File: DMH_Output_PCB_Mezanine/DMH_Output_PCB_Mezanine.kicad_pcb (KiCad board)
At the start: 2 copper layers, 49 x 175 mm, 105 parts, among them J30 Conn_01x04_PinHeader, J32 Conn_01x06_PinHeader, J33 Conn_01x06, J34 Conn_01x06, J37 Conn_01x06, J38 Conn_01x06, J39 Conn_01x02_PinHeader, J40 Conn_01x02_PinHeader, U10 NE5532, U16 NE5532, U17 NE5532, U18 NE5532, U19 NE5532, U7 TL072, U9 NE5532

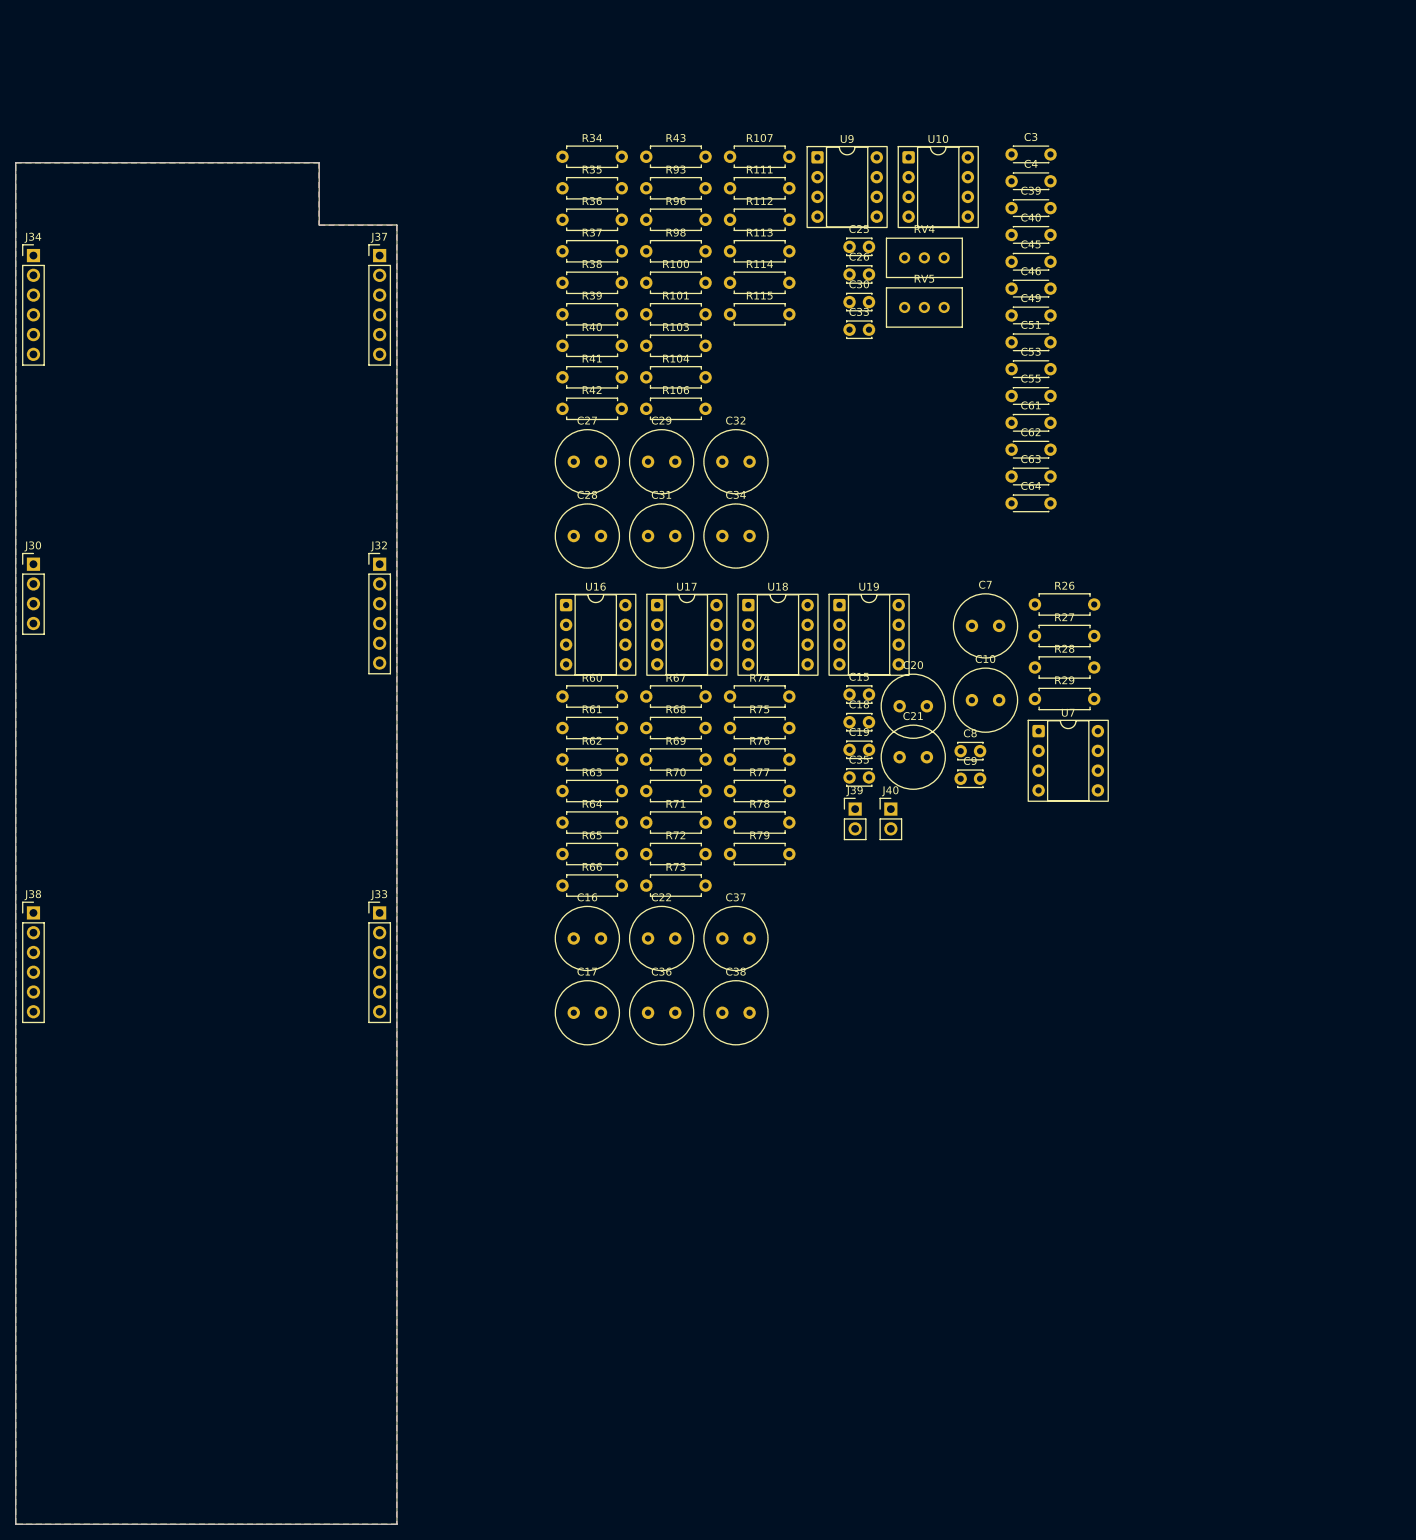
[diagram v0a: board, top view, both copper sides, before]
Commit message: Defined Mezanine PCB outer limits
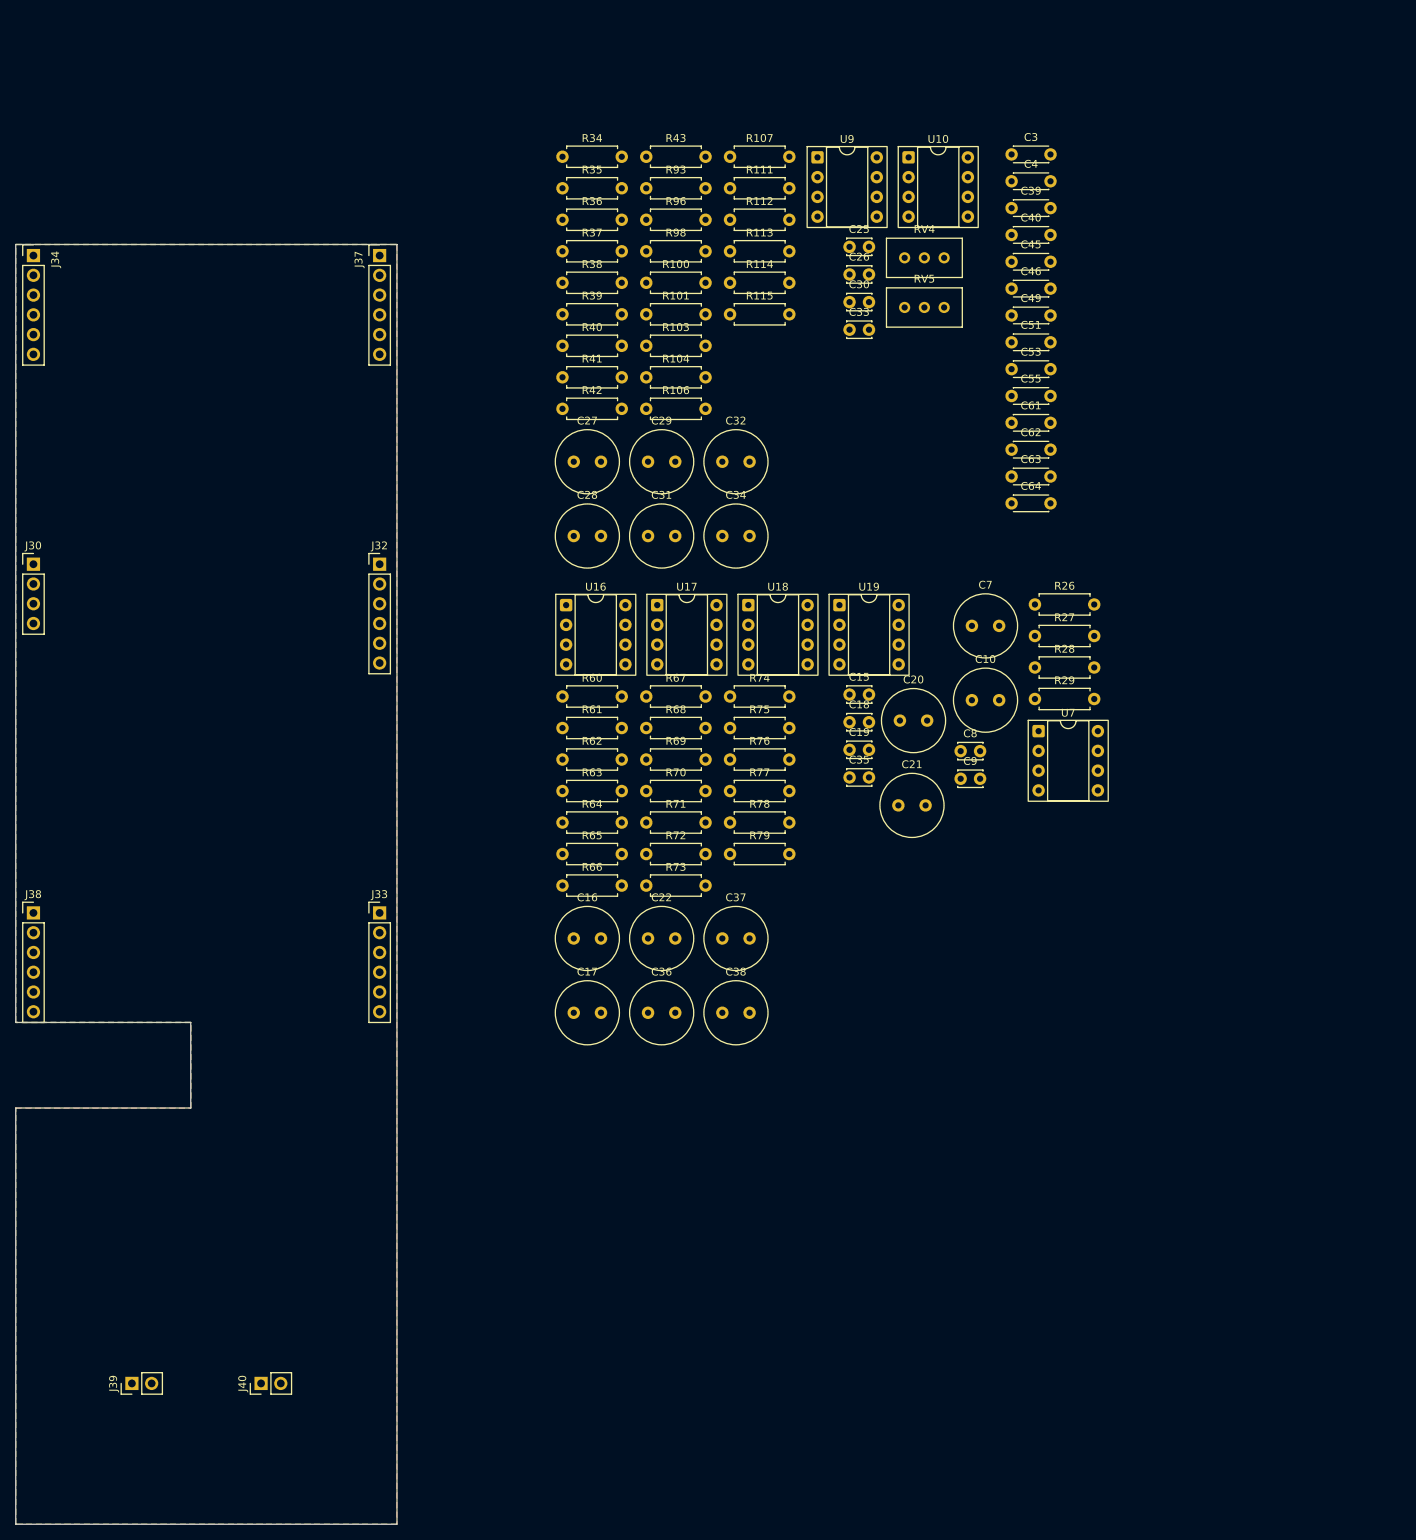
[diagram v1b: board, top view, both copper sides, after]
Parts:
- moved J39 118.7 mm to (65.4, 199.4), turned to 90 degrees
- moved J40 109.6 mm to (82.0, 199.4), turned to 90 degrees
- moved C21 6.20 mm to (163.9, 125.1)
- moved C20 1.85 mm to (164.2, 114.2)
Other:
- board size 49 x 175 mm -> 49 x 164.5 mm
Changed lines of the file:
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@@
 	)
 	(footprint "Connector_PinHeader_2.54mm:PinHeader_1x02_P2.54mm_Vertical"
+		(locked yes)
 		(layer "F.Cu")
-		(at 162.985 125.575)
+		(at 82.03 199.4 90)
 		(descr "Through hole straight pin header, 1x02, 2.54mm pitch, single row")
 		(tags "Through hole pin header THT 1x02 2.54mm single row")
 		(property "Reference" "J40"
-			(at 0 -2.38 0)
+			(at 0 -2.38 90)
 			(layer "F.SilkS")
 			(effects
@@
 		)
 		(property "Value" "Conn_01x02_PinHeader"
-			(at 0 4.92 0)
+			(at 0 4.92 90)
 			(layer "F.Fab")
 			(hide yes)
@@
 		)
 		(property "Datasheet" ""
-			(at 0 0 0)
+			(at 0 0 90)
 			(layer "F.Fab")
 			(hide yes)
@@
 		)
 		(property "Description" "Generic connector, single row, 01x02"
-			(at 0 0 0)
+			(at 0 0 90)
 			(layer "F.Fab")
 			(hide yes)
@@
 		)
 		(property "KiLib_Generator" "connector/pin_header_socket"
-			(at 0 0 0)
+			(at 0 0 90)
 			(layer "F.SilkS")
 			(hide yes)
@@
 		)
 		(fp_line
-			(start -1.38 1.27)
-			(end -1.38 3.92)
+			(start 1.38 1.27)
+			(end 1.38 3.92)
 			(stroke
 				(width 0.12)
@@
 		)
 		(fp_line
-			(start -1.38 3.92)
-			(end 1.38 3.92)
+			(start -1.38 1.27)
+			(end -1.38 3.92)
 			(stroke
 				(width 0.12)
@@
 		)
 		(fp_line
-			(start 1.38 1.27)
+			(start -1.38 3.92)
 			(end 1.38 3.92)
 			(stroke
@@
 		)
 		(fp_line
-			(start -1.27 -0.635)
-			(end -0.635 -1.27)
+			(start 1.27 -1.27)
+			(end 1.27 3.81)
 			(stroke
 				(width 0.1)
@@
 		)
 		(fp_line
-			(start -1.27 3.81)
-			(end -1.27 -0.635)
+			(start -0.635 -1.27)
+			(end 1.27 -1.27)
 			(stroke
 				(width 0.1)
@@
 		)
 		(fp_line
-			(start -0.635 -1.27)
-			(end 1.27 -1.27)
+			(start -1.27 -0.635)
+			(end -0.635 -1.27)
 			(stroke
 				(width 0.1)
@@
 		)
 		(fp_line
-			(start 1.27 -1.27)
-			(end 1.27 3.81)
+			(start 1.27 3.81)
+			(end -1.27 3.81)
 			(stroke
 				(width 0.1)
@@
 		)
 		(fp_line
-			(start 1.27 3.81)
-			(end -1.27 3.81)
+			(start -1.27 3.81)
+			(end -1.27 -0.635)
 			(stroke
 				(width 0.1)
@@
 		)
 		(fp_text user "${REFERENCE}"
-			(at 0 1.27 90)
+			(at 0 1.27 0)
 			(layer "F.Fab")
 			(effects
@@
 		)
 		(pad "1" thru_hole rect
-			(at 0 0)
+			(at 0 0 90)
 			(size 1.7 1.7)
 			(drill 1)
@@
 		)
 		(pad "2" thru_hole circle
-			(at 0 2.54)
+			(at 0 2.54 90)
 			(size 1.7 1.7)
 			(drill 1)
@@
 	(footprint "Capacitor_THT:C_Radial_D8.0mm_H11.5mm_P3.50mm"
 		(layer "F.Cu")
-		(at 164.114775 118.905)
+		(at 163.95 125.1)
 		(descr "C, Radial series, Radial, pin pitch=3.50mm, diameter=8mm, height=11.5mm, Non-Polar Electrolytic Capacitor")
 		(tags "C Radial series Radial pin pitch 3.50mm diameter 8mm height 11.5mm Non-Polar Electrolytic Capacitor")
@@
 		(tags "Through hole pin header THT 1x06 2.54mm single row")
 		(property "Reference" "J37"
-			(at 0 -2.38 0)
+			(at -2.675 0.475 90)
 			(layer "F.SilkS")
 			(effects
@@
 		(tags "Through hole pin header THT 1x06 2.54mm single row")
 		(property "Reference" "J34"
-			(at 0 -2.38 0)
+			(at 2.825 0.475 90)
 			(layer "F.SilkS")
 			(effects
@@
 	)
 	(footprint "Connector_PinHeader_2.54mm:PinHeader_1x02_P2.54mm_Vertical"
+		(locked yes)
 		(layer "F.Cu")
-		(at 158.395 125.575)
+		(at 65.43 199.4 90)
 		(descr "Through hole straight pin header, 1x02, 2.54mm pitch, single row")
 		(tags "Through hole pin header THT 1x02 2.54mm single row")
 		(property "Reference" "J39"
-			(at 0 -2.38 0)
+			(at 0 -2.38 90)
 			(layer "F.SilkS")
 			(effects
@@
 		)
 		(property "Value" "Conn_01x02_PinHeader"
-			(at 0 4.92 0)
+			(at 0 4.92 90)
 			(layer "F.Fab")
 			(hide yes)
@@
 		)
 		(property "Datasheet" ""
-			(at 0 0 0)
+			(at 0 0 90)
 			(layer "F.Fab")
 			(hide yes)
@@
 		)
 		(property "Description" "Generic connector, single row, 01x02"
-			(at 0 0 0)
+			(at 0 0 90)
 			(layer "F.Fab")
 			(hide yes)
@@
 		)
 		(property "KiLib_Generator" "connector/pin_header_socket"
-			(at 0 0 0)
+			(at 0 0 90)
 			(layer "F.SilkS")
 			(hide yes)
@@
 		)
 		(fp_line
-			(start -1.38 1.27)
-			(end -1.38 3.92)
+			(start 1.38 1.27)
+			(end 1.38 3.92)
 			(stroke
 				(width 0.12)
@@
 		)
 		(fp_line
-			(start -1.38 3.92)
-			(end 1.38 3.92)
+			(start -1.38 1.27)
+			(end -1.38 3.92)
 			(stroke
 				(width 0.12)
@@
 		)
 		(fp_line
-			(start 1.38 1.27)
+			(start -1.38 3.92)
 			(end 1.38 3.92)
 			(stroke
@@
 		)
 		(fp_line
-			(start -1.27 -0.635)
-			(end -0.635 -1.27)
+			(start 1.27 -1.27)
+			(end 1.27 3.81)
 			(stroke
 				(width 0.1)
@@
 		)
 		(fp_line
-			(start -1.27 3.81)
-			(end -1.27 -0.635)
+			(start -0.635 -1.27)
+			(end 1.27 -1.27)
 			(stroke
 				(width 0.1)
@@
 		)
 		(fp_line
-			(start -0.635 -1.27)
-			(end 1.27 -1.27)
+			(start -1.27 -0.635)
+			(end -0.635 -1.27)
 			(stroke
 				(width 0.1)
@@
 		)
 		(fp_line
-			(start 1.27 -1.27)
-			(end 1.27 3.81)
+			(start 1.27 3.81)
+			(end -1.27 3.81)
 			(stroke
 				(width 0.1)
@@
 		)
 		(fp_line
-			(start 1.27 3.81)
-			(end -1.27 3.81)
+			(start -1.27 3.81)
+			(end -1.27 -0.635)
 			(stroke
 				(width 0.1)
@@
 		)
 		(fp_text user "${REFERENCE}"
-			(at 0 1.27 90)
+			(at 0 1.27 0)
 			(layer "F.Fab")
 			(effects
@@
 		)
 		(pad "1" thru_hole rect
-			(at 0 0)
+			(at 0 0 90)
 			(size 1.7 1.7)
 			(drill 1)
@@
 		)
 		(pad "2" thru_hole circle
-			(at 0 2.54)
+			(at 0 2.54 90)
 			(size 1.7 1.7)
 			(drill 1)
@@
 	(footprint "Capacitor_THT:C_Radial_D8.0mm_H11.5mm_P3.50mm"
 		(layer "F.Cu")
-		(at 164.114775 112.355)
+		(at 164.15 114.2)
 		(descr "C, Radial series, Radial, pin pitch=3.50mm, diameter=8mm, height=11.5mm, Non-Polar Electrolytic Capacitor")
 		(tags "C Radial series Radial pin pitch 3.50mm diameter 8mm height 11.5mm Non-Polar Electrolytic Capacitor")
@@
 	)
 	(gr_line
-		(start 50.5 42.5)
-		(end 89.5 42.5)
+		(start 50.5 53)
+		(end 99.5 53)
+		(stroke
+			(width 0.05)
+			(type default)
+		)
+		(layer "Edge.Cuts")
+	)
+	(gr_line
+		(start 50.5 153)
+		(end 50.5 53)
+		(stroke
+			(width 0.05)
+			(type default)
+		)
+		(layer "Edge.Cuts")
+	)
+	(gr_line
+		(start 50.5 153)
+		(end 73 153)
 		(stroke
 			(width 0.05)
@@
 	(gr_line
 		(start 50.5 217.5)
-		(end 50.5 42.5)
+		(end 50.5 164)
 		(stroke
 			(width 0.05)
@@
 	)
 	(gr_line
-		(start 89.5 42.5)
-		(end 89.5 50.5)
+		(start 73 153)
+		(end 73 164)
 		(stroke
 			(width 0.05)
@@
 	)
 	(gr_line
-		(start 89.5 50.5)
-		(end 99.5 50.5)
+		(start 73 164)
+		(end 50.5 164)
 		(stroke
 			(width 0.05)
@@
 	)
 	(gr_line
-		(start 99.5 50.5)
+		(start 99.5 53)
 		(end 99.5 217.5)
 		(stroke
@@
 		(net "GND")
 		(layers "F.Cu" "B.Cu")
-		(name "Ground_planes")
+		(name "Ground_planes")
 		(hatch edge 0.5)
 		(connect_pads
@@
 		(polygon
 			(pts
-				(xy 50.5 42.5) (xy 89.5 42.5) (xy 89.5 50.5) (xy 99.5 50.5) (xy 99.5 217.5) (xy 50.5 217.5)
+				(xy 50.5 53) (xy 99.5 53) (xy 99.5 217.5) (xy 50.5 217.5) (xy 50.5 164) (xy 73 164) (xy 73 153)
+				(xy 50.5 153)
 			)
 		)

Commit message: Placed PreAmp components on PCB
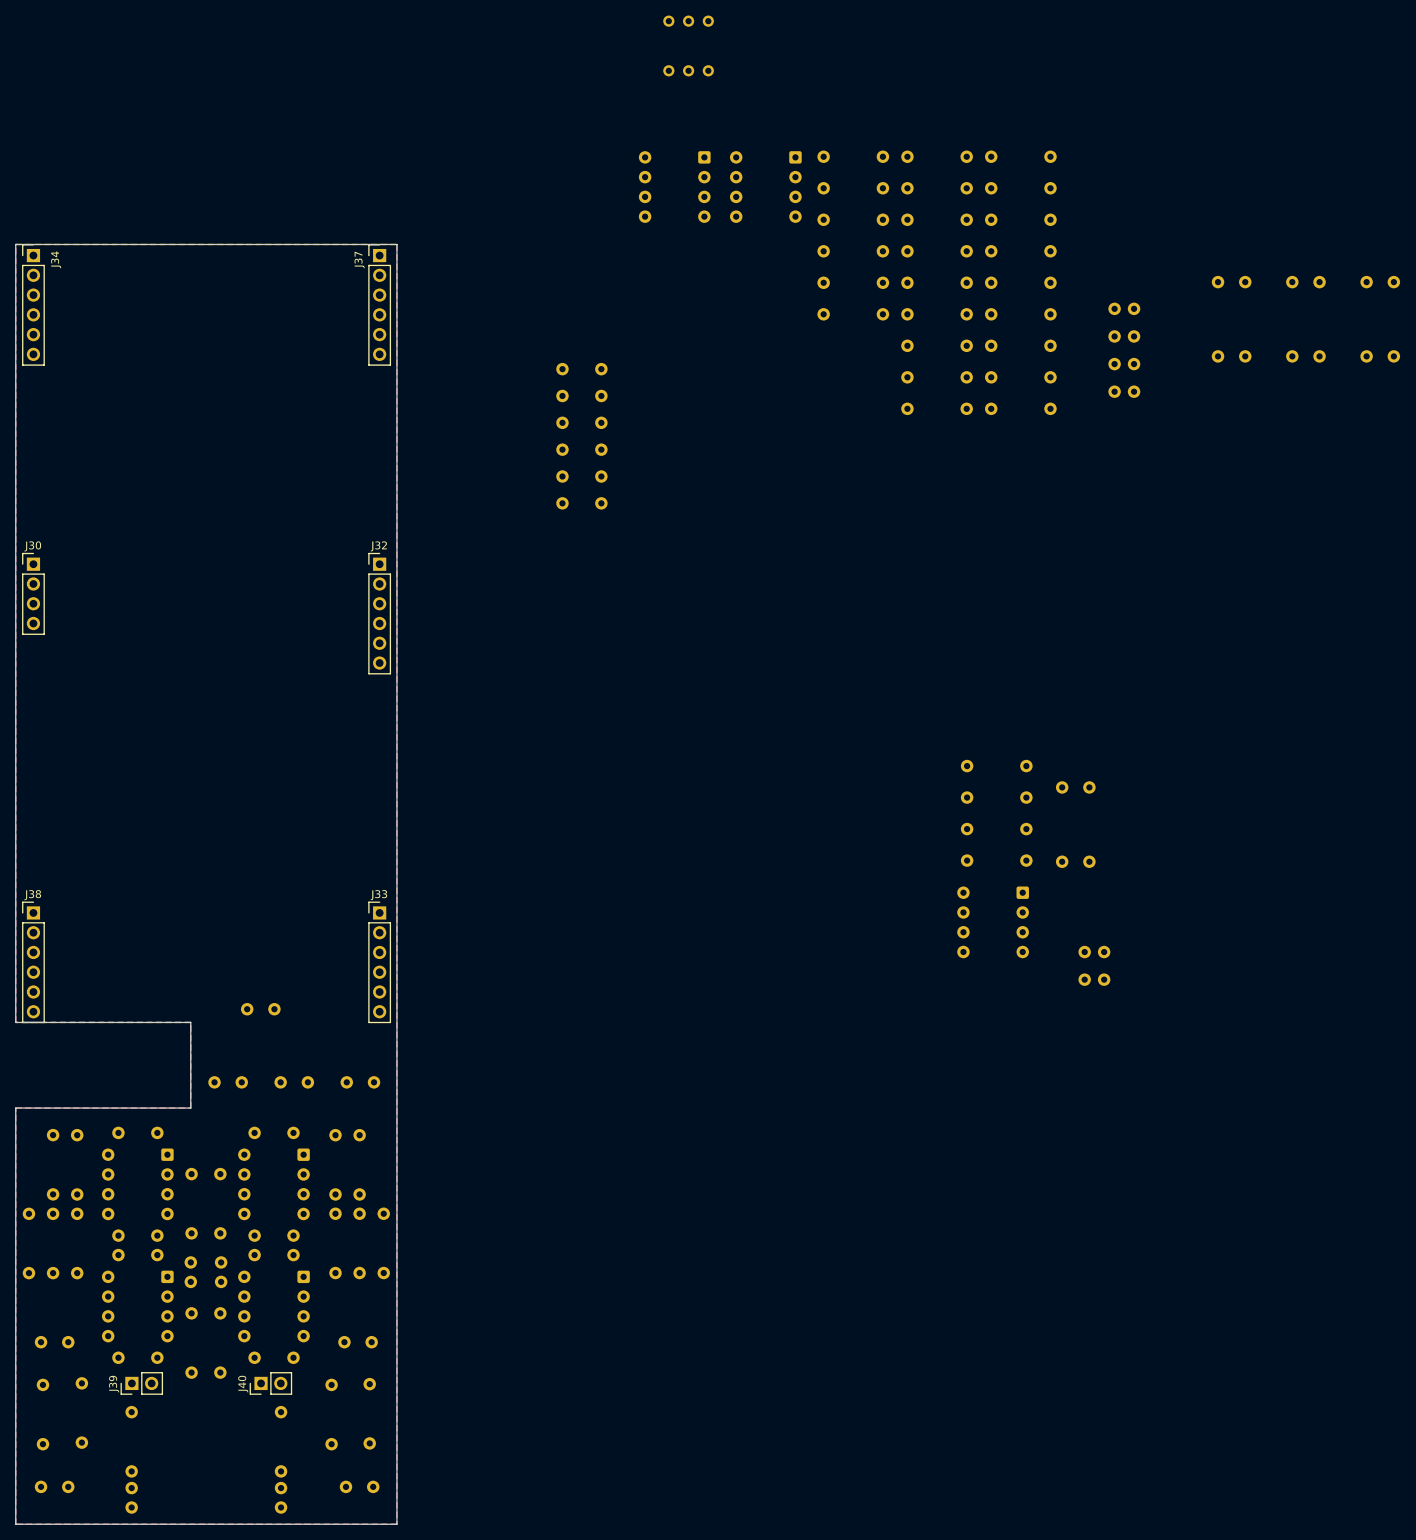
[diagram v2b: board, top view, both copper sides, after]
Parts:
- C10, C15, C16, C17, C18, C19, C20, C21, C22, C25, C26, C27, C28, C29, C3, C30, C31, C32, C33, C34, C35, C36, C37, C38, C39, C4, C40, C45, C46, C49, C51, C53, C55, C61, C62, C63, C64, C7, C8, C9, R100, R101, R103, R104, R106, R107, R111, R112, R113, R114, R115, R26, R27, R28, R29, R34, R35, R36, R37, R38, R39, R40, R41, R42, R43, R60, R61, R62, R63, R64, R65, R66, R67, R68, R69, R70, R71, R72, R73, R74, R75, R76, R77, R78, R79, R93, R96, R98, RV4, RV5, U10, U16, U17, U18, U19, U7, U9: moved to B.Cu
- moved C40 184.4 mm to (63.7, 196.1)
- moved C4 177.6 mm to (63.7, 180.4)
- moved C39 176.9 mm to (63.7, 182.9)
- moved C3 170.3 mm to (63.7, 167.2)
- moved C51 162.8 mm to (81.2, 196.1)
- moved C46 155.8 mm to (81.2, 180.4)
- moved C49 155.1 mm to (81.2, 182.9)
- moved C45 148.3 mm to (81.2, 167.2)
- moved C18 136.8 mm to (65.4, 215.3), turned to 90 degrees
- moved C15 127.5 mm to (84.6, 215.3), turned to 90 degrees
- moved U19 110.5 mm to (87.5, 185.7), turned to 180 degrees
- moved C27 107.9 mm to (227.6, 57.8), turned to 180 degrees
- moved C28 107.9 mm to (227.6, 67.4), turned to 180 degrees
- moved C19 107.3 mm to (73.0, 183.8), turned to -90 degrees
- moved U17 106.9 mm to (70.0, 185.7), turned to 180 degrees
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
